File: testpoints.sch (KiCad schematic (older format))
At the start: 22 parts

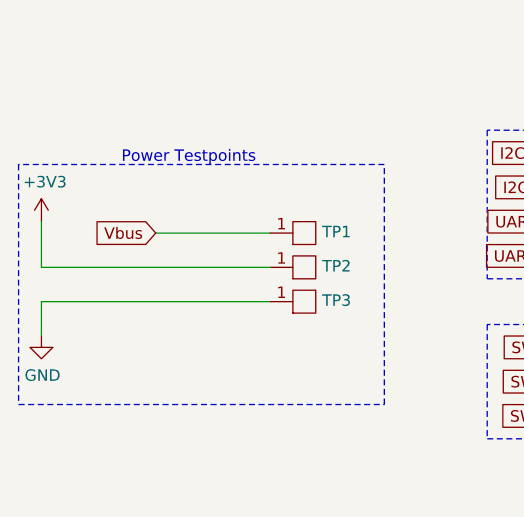
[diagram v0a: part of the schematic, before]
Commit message: Initial layout complete. Pins moved to make layout easy
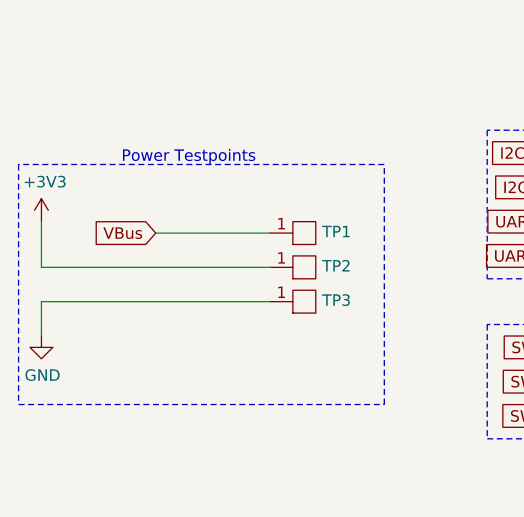
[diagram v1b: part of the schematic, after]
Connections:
- net Vbus renamed VBus
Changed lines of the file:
@@
 $EndDescr
 Text GLabel 3650 3350 0    50   Input ~ 0
-Vbus
+VBus
 $Comp
 L power:+3V3 #PWR?
